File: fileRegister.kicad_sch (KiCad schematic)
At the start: 12 parts

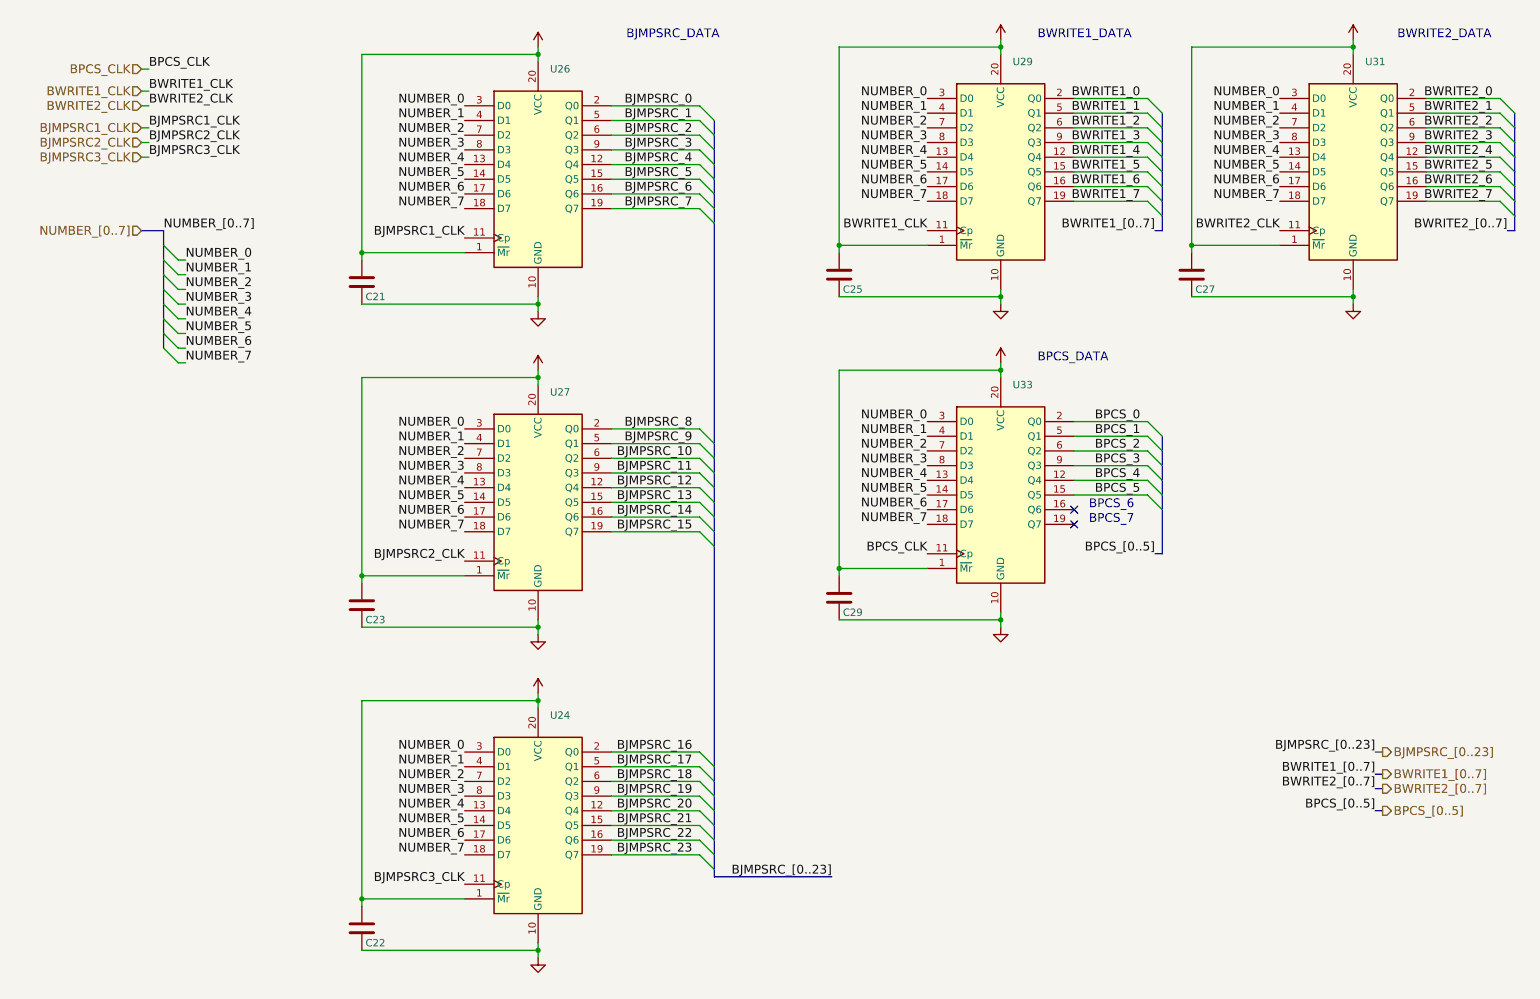
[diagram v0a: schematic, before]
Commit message: Updating descriptions
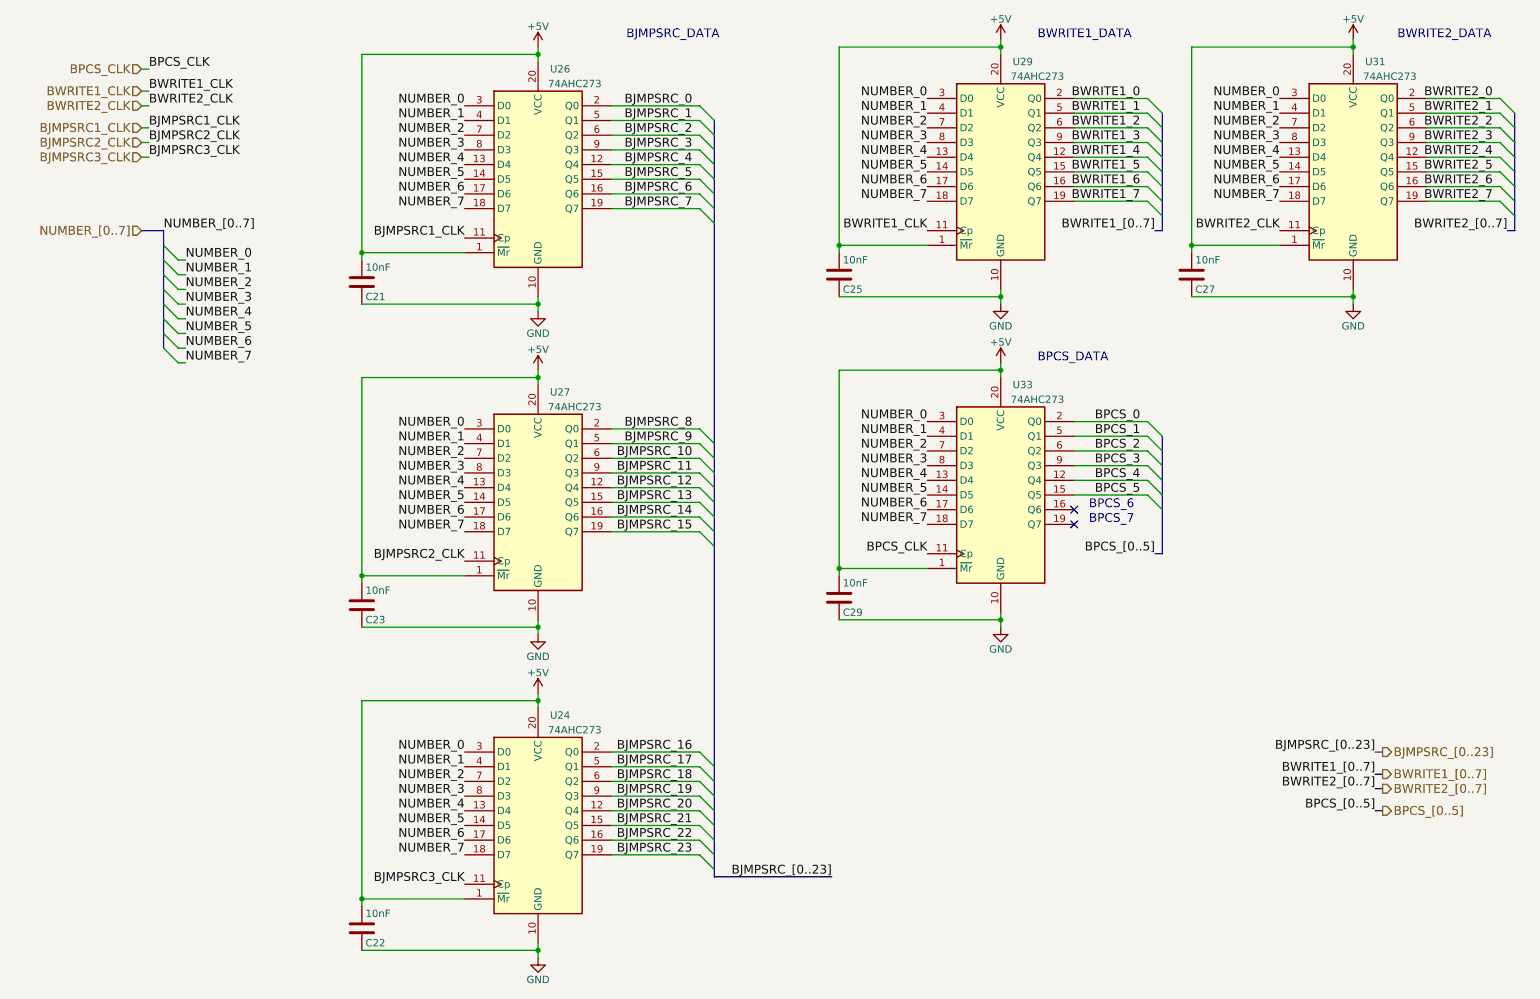
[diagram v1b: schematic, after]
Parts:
- C21, C22, C23, C25, C27, C29: value (none) -> 10nF; footprint (none) -> Capacitor_SMD:C_0805_2012Metric
- U24, U26, U27, U29, U31, U33: value (none) -> 74AHC273; footprint (none) -> Package_SO:SOIC-20W_7.5x12.8mm_P1.27mm
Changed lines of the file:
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@@
   (title_block
     (title "GP8B")
-    (date "2021-03-04")
-    (rev "V5.1")
+    (date "2022-07-08")
+    (rev "V6.0")
     (company "Guillaume Guillet")
-    (comment 1 "Copyright Guillaume Guillet 2021")
+    (comment 1 "Copyright Guillaume Guillet 2022")
     (comment 2 "Licensed under CERN-OHL-W v2 or later")
   )
@@
       (effects (font (size 1.27 1.27)) hide)
     )
-    (property "Value" "" (id 1) (at 243.84 18.034 0))
+    (property "Value" "+5V" (id 1) (at 243.84 18.034 0))
     (property "Footprint" "" (id 2) (at 243.84 21.59 0)
       (effects (font (size 1.27 1.27)) hide)
@@
       (effects (font (size 1.27 1.27)) hide)
     )
-    (property "Value" "" (id 1) (at 182.88 18.034 0))
+    (property "Value" "+5V" (id 1) (at 182.88 18.034 0))
     (property "Footprint" "" (id 2) (at 182.88 21.59 0)
       (effects (font (size 1.27 1.27)) hide)
@@
       (effects (font (size 1.27 1.27)) hide)
     )
-    (property "Value" "" (id 1) (at 182.88 71.12 0))
+    (property "Value" "GND" (id 1) (at 182.88 71.12 0))
     (property "Footprint" "" (id 2) (at 182.88 67.31 0)
       (effects (font (size 1.27 1.27)) hide)
@@
       (effects (font (size 1.27 1.27)) hide)
     )
-    (property "Value" "" (id 1) (at 243.84 71.12 0))
+    (property "Value" "GND" (id 1) (at 243.84 71.12 0))
     (property "Footprint" "" (id 2) (at 243.84 67.31 0)
       (effects (font (size 1.27 1.27)) hide)
@@
       (effects (font (size 1.27 1.27)) (justify left))
     )
-    (property "Value" "" (id 1) (at 155.575 59.69 0)
+    (property "Value" "10nF" (id 1) (at 155.575 59.69 0)
       (effects (font (size 1.27 1.27)) (justify left))
     )
-    (property "Footprint" "" (id 2) (at 155.9052 58.42 0)
+    (property "Footprint" "Capacitor_SMD:C_0805_2012Metric" (id 2) (at 155.9052 58.42 0)
       (effects (font (size 1.27 1.27)) hide)
     )
@@
       (effects (font (size 1.27 1.27)) (justify left))
     )
-    (property "Value" "" (id 1) (at 216.535 59.69 0)
+    (property "Value" "10nF" (id 1) (at 216.535 59.69 0)
       (effects (font (size 1.27 1.27)) (justify left))
     )
-    (property "Footprint" "" (id 2) (at 216.8652 58.42 0)
+    (property "Footprint" "Capacitor_SMD:C_0805_2012Metric" (id 2) (at 216.8652 58.42 0)
       (effects (font (size 1.27 1.27)) hide)
     )
@@
       (effects (font (size 1.27 1.27)) hide)
     )
-    (property "Value" "" (id 1) (at 182.88 73.914 0))
+    (property "Value" "+5V" (id 1) (at 182.88 73.914 0))
     (property "Footprint" "" (id 2) (at 182.88 77.47 0)
       (effects (font (size 1.27 1.27)) hide)
@@
       (effects (font (size 1.27 1.27)) hide)
     )
-    (property "Value" "" (id 1) (at 182.88 127 0))
+    (property "Value" "GND" (id 1) (at 182.88 127 0))
     (property "Footprint" "" (id 2) (at 182.88 123.19 0)
       (effects (font (size 1.27 1.27)) hide)
@@
       (effects (font (size 1.27 1.27)) (justify left))
     )
-    (property "Value" "" (id 1) (at 155.575 115.57 0)
+    (property "Value" "10nF" (id 1) (at 155.575 115.57 0)
       (effects (font (size 1.27 1.27)) (justify left))
     )
-    (property "Footprint" "" (id 2) (at 155.9052 114.3 0)
+    (property "Footprint" "Capacitor_SMD:C_0805_2012Metric" (id 2) (at 155.9052 114.3 0)
       (effects (font (size 1.27 1.27)) hide)
     )
@@
       (effects (font (size 1.27 1.27)) hide)
     )
-    (property "Value" "" (id 1) (at 102.87 75.184 0))
+    (property "Value" "+5V" (id 1) (at 102.87 75.184 0))
     (property "Footprint" "" (id 2) (at 102.87 78.74 0)
       (effects (font (size 1.27 1.27)) hide)
@@
       (effects (font (size 1.27 1.27)) hide)
     )
-    (property "Value" "" (id 1) (at 102.87 19.304 0))
+    (property "Value" "+5V" (id 1) (at 102.87 19.304 0))
     (property "Footprint" "" (id 2) (at 102.87 22.86 0)
       (effects (font (size 1.27 1.27)) hide)
@@
       (effects (font (size 1.27 1.27)) hide)
     )
-    (property "Value" "" (id 1) (at 102.87 72.39 0))
+    (property "Value" "GND" (id 1) (at 102.87 72.39 0))
     (property "Footprint" "" (id 2) (at 102.87 68.58 0)
       (effects (font (size 1.27 1.27)) hide)
@@
       (effects (font (size 1.27 1.27)) hide)
     )
-    (property "Value" "" (id 1) (at 102.87 128.27 0))
+    (property "Value" "GND" (id 1) (at 102.87 128.27 0))
     (property "Footprint" "" (id 2) (at 102.87 124.46 0)
       (effects (font (size 1.27 1.27)) hide)
@@
       (effects (font (size 1.27 1.27)) (justify left))
     )
-    (property "Value" "" (id 1) (at 73.025 60.96 0)
+    (property "Value" "10nF" (id 1) (at 73.025 60.96 0)
       (effects (font (size 1.27 1.27)) (justify left))
     )
-    (property "Footprint" "" (id 2) (at 73.3552 59.69 0)
+    (property "Footprint" "Capacitor_SMD:C_0805_2012Metric" (id 2) (at 73.3552 59.69 0)
       (effects (font (size 1.27 1.27)) hide)
     )
@@
       (effects (font (size 1.27 1.27)) (justify left))
     )
-    (property "Value" "" (id 1) (at 73.025 116.84 0)
+    (property "Value" "10nF" (id 1) (at 73.025 116.84 0)
       (effects (font (size 1.27 1.27)) (justify left))
     )
-    (property "Footprint" "" (id 2) (at 73.3552 115.57 0)
+    (property "Footprint" "Capacitor_SMD:C_0805_2012Metric" (id 2) (at 73.3552 115.57 0)
       (effects (font (size 1.27 1.27)) hide)
     )
@@
       (effects (font (size 1.27 1.27)) hide)
     )
-    (property "Value" "" (id 1) (at 102.87 131.064 0))
+    (property "Value" "+5V" (id 1) (at 102.87 131.064 0))
     (property "Footprint" "" (id 2) (at 102.87 134.62 0)
       (effects (font (size 1.27 1.27)) hide)
@@
       (effects (font (size 1.27 1.27)) hide)
     )
-    (property "Value" "" (id 1) (at 102.87 184.15 0))
+    (property "Value" "GND" (id 1) (at 102.87 184.15 0))
     (property "Footprint" "" (id 2) (at 102.87 180.34 0)
       (effects (font (size 1.27 1.27)) hide)
@@
       (effects (font (size 1.27 1.27)) (justify left))
     )
-    (property "Value" "" (id 1) (at 73.025 172.72 0)
+    (property "Value" "10nF" (id 1) (at 73.025 172.72 0)
       (effects (font (size 1.27 1.27)) (justify left))
     )
-    (property "Footprint" "" (id 2) (at 73.3552 171.45 0)
+    (property "Footprint" "Capacitor_SMD:C_0805_2012Metric" (id 2) (at 73.3552 171.45 0)
       (effects (font (size 1.27 1.27)) hide)
     )
@@
     (in_bom yes) (on_board yes)
     (property "Reference" "U29" (id 0) (at 186.69 25.4 0))
-    (property "Value" "" (id 1) (at 189.23 27.94 0))
-    (property "Footprint" "" (id 2) (at 182.88 44.45 0)
+    (property "Value" "74AHC273" (id 1) (at 189.23 27.94 0))
+    (property "Footprint" "Package_SO:SOIC-20W_7.5x12.8mm_P1.27mm" (id 2) (at 182.88 44.45 0)
       (effects (font (size 1.27 1.27)) hide)
     )
@@
     (in_bom yes) (on_board yes)
     (property "Reference" "U31" (id 0) (at 247.65 25.4 0))
-    (property "Value" "" (id 1) (at 250.19 27.94 0))
-    (property "Footprint" "" (id 2) (at 243.84 44.45 0)
+    (property "Value" "74AHC273" (id 1) (at 250.19 27.94 0))
+    (property "Footprint" "Package_SO:SOIC-20W_7.5x12.8mm_P1.27mm" (id 2) (at 243.84 44.45 0)
       (effects (font (size 1.27 1.27)) hide)
     )
@@
     (in_bom yes) (on_board yes)
     (property "Reference" "U33" (id 0) (at 186.69 81.28 0))
-    (property "Value" "" (id 1) (at 189.23 83.82 0))
-    (property "Footprint" "" (id 2) (at 182.88 100.33 0)
+    (property "Value" "74AHC273" (id 1) (at 189.23 83.82 0))
+    (property "Footprint" "Package_SO:SOIC-20W_7.5x12.8mm_P1.27mm" (id 2) (at 182.88 100.33 0)
       (effects (font (size 1.27 1.27)) hide)
     )
@@
     (in_bom yes) (on_board yes)
     (property "Reference" "U26" (id 0) (at 106.68 26.67 0))
-    (property "Value" "" (id 1) (at 109.22 29.21 0))
-    (property "Footprint" "" (id 2) (at 102.87 45.72 0)
+    (property "Value" "74AHC273" (id 1) (at 109.22 29.21 0))
+    (property "Footprint" "Package_SO:SOIC-20W_7.5x12.8mm_P1.27mm" (id 2) (at 102.87 45.72 0)
       (effects (font (size 1.27 1.27)) hide)
     )
@@
     (in_bom yes) (on_board yes)
     (property "Reference" "U24" (id 0) (at 106.68 138.43 0))
-    (property "Value" "" (id 1) (at 109.22 140.97 0))
-    (property "Footprint" "" (id 2) (at 102.87 157.48 0)
+    (property "Value" "74AHC273" (id 1) (at 109.22 140.97 0))
+    (property "Footprint" "Package_SO:SOIC-20W_7.5x12.8mm_P1.27mm" (id 2) (at 102.87 157.48 0)
       (effects (font (size 1.27 1.27)) hide)
     )
@@
     (in_bom yes) (on_board yes)
     (property "Reference" "U27" (id 0) (at 106.68 82.55 0))
-    (property "Value" "" (id 1) (at 109.22 85.09 0))
-    (property "Footprint" "" (id 2) (at 102.87 101.6 0)
-      (effects (font (size 1.27 1.27)) hide)
-    )
+    (property "Value" "74AHC273" (id 1) (at 109.22 85.09 0))
+    (property "Footprint" "Package_SO:SOIC-20W_7.5x12.8mm_P1.27mm" (id 2) (at 102.87 101.6 0)
+      (effects (font (size 1.27 1.27)) hide)
+    )
